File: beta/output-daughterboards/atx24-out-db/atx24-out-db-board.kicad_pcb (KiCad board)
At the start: 4 copper layers, 55 x 21.4 mm, 13 parts, among them J1 ATX24 OUT FIELD, J10 TE 63951-1, J11 TE 63951-1, J12 TE 63951-1, J13 TE 63951-1, J14 TE 63951-1, J15 TE 63951-1, J16 TE 63951-1, J17 TE 63951-1, J18 TE 63951-1, J19 TE 63951-1, J20 SIGNAL STUB (1x4 blind-mate)

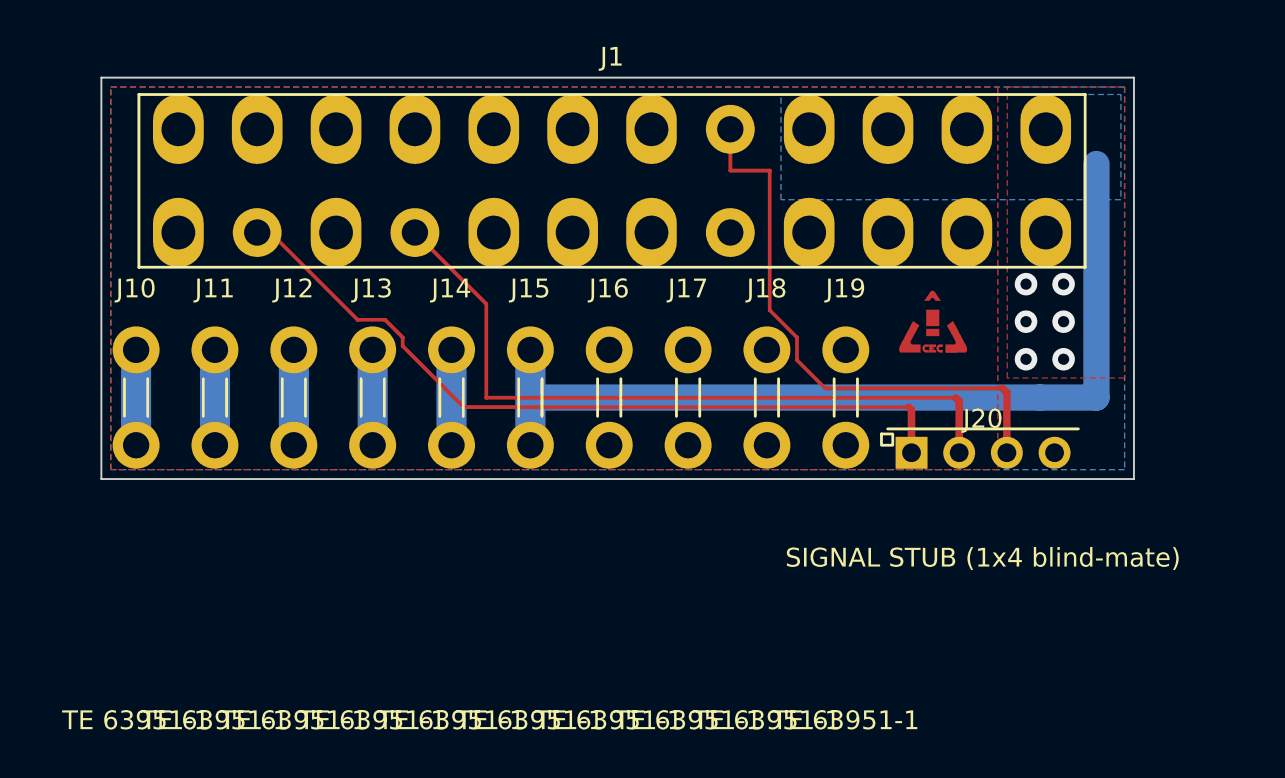
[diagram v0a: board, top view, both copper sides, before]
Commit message: Finalize compact Hub and ATX power-layout audit
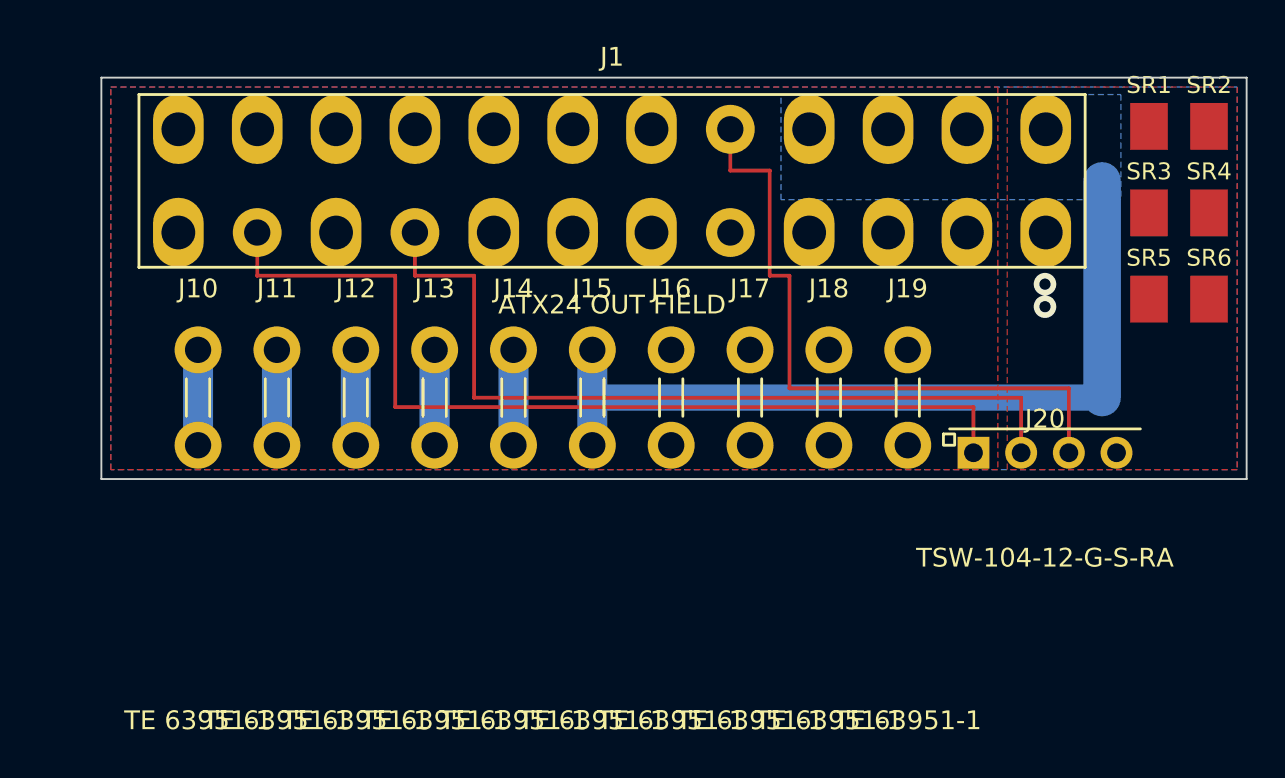
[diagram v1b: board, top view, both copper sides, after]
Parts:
- removed LOGO1: CEC_Logo_Copper_Small, cec:CEC_Logo_Copper_Small
- added SR1: SR_DNP, cec-Connector_Generic:CEC_SR_Pad_DNP, F.Cu at (55.8, 2.60)
- added SR2: SR_DNP, cec-Connector_Generic:CEC_SR_Pad_DNP, F.Cu at (59.0, 2.60)
- added SR3: SR_DNP, cec-Connector_Generic:CEC_SR_Pad_DNP, F.Cu at (55.8, 7.20)
- added SR4: SR_DNP, cec-Connector_Generic:CEC_SR_Pad_DNP, F.Cu at (59.0, 7.20)
- added SR5: SR_DNP, cec-Connector_Generic:CEC_SR_Pad_DNP, F.Cu at (55.8, 11.8)
- added SR6: SR_DNP, cec-Connector_Generic:CEC_SR_Pad_DNP, F.Cu at (59.0, 11.8)
- J20: value SIGNAL STUB (1x4 blind-mate) -> TSW-104-12-G-S-RA
- moved J19 3.30 mm to (43.0, 17.0)
- moved J20 3.30 mm to (46.5, 20.0)
- moved J12 3.30 mm to (13.6, 17.0)
- moved J13 3.30 mm to (17.8, 17.0)
- moved J14 3.30 mm to (21.9, 17.0)
- moved J16 3.30 mm to (30.4, 17.0)
- moved J10 3.30 mm to (5.15, 17.0)
- moved J11 3.30 mm to (9.35, 17.0)
- moved J15 3.30 mm to (26.1, 17.0)
- moved J17 3.30 mm to (34.5, 17.0)
- moved J18 3.30 mm to (38.8, 17.0)
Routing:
- net /-12V: track 41.3 -> 49.9 mm
- net /PS_ON#: track 38.4 -> 44.0 mm
- net /PWR_OK: track 30.1 -> 35.3 mm
- net +5VSB: track 47.7 -> 43.8 mm
- net +3V3: vias 6 -> 2
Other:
- board size 55 x 21.4 mm -> 61 x 21.4 mm

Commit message: pipeline: integrate route-aware physical design flow
Generalize critical-first placement and routing, future-congestion and power-authority planning, route provenance, process watchdogs, fab/thermal validation, dashboard review, and XFCN integration. Add the supporting board contracts, component libraries, documentation, and regression coverage.
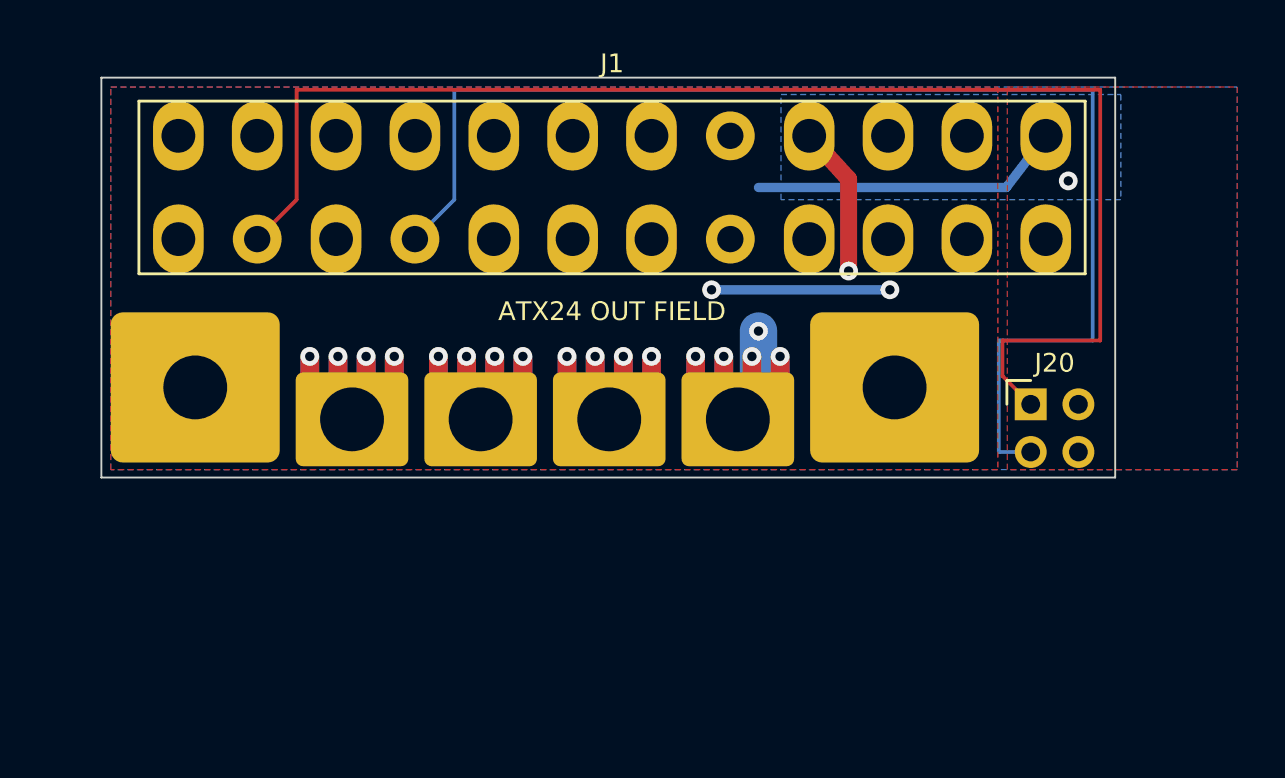
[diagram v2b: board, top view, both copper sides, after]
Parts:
- removed J12, J14, J17, J18: TE 63951-1, cec-Connector_Blade:TE_63951-1_FASTON_Tab_250x032_RA_THT
- removed SR1, SR2, SR3, SR4, SR5, SR6: SR_DNP, cec-Connector_Generic:CEC_SR_Pad_DNP
- J10, J11, J13, J15: value TE 63951-1 -> T34069 DB M3 PAD; footprint cec-Connector_Blade:TE_63951-1_FASTON_Tab_250x032_RA_THT -> cec-Connector_Screw:XFCN_T34069_Daughterboard_BoltPad_M3_PROVISIONAL
- J16, J19: value TE 63951-1 -> TTR32100127-0600 DB M3 PAD; footprint cec-Connector_Blade:TE_63951-1_FASTON_Tab_250x032_RA_THT -> cec-Connector_Screw:XFCN_TTR32100127-0600_Daughterboard_BoltPad_M3_PROVISIONAL
- J20: value TSW-104-12-G-S-RA -> TSW-102-16-G-D-RA; footprint cec-Connector_PinHeader_2.54mm:PinHeader_1x04_P2.54mm_Horizontal_LongPin -> cec-Connector_PinHeader_2.54mm:Samtec_TSW-102-16-G-D-RA_2x02_P2.54mm_Horizontal
- moved J16 25.4 mm to (5.00, 16.5)
- moved J10 21.9 mm to (27.1, 18.2)
- moved J11 10.9 mm to (20.2, 18.2)
- moved J15 7.84 mm to (33.9, 18.2)
- moved J13 4.55 mm to (13.3, 18.2)
- moved J20 3.99 mm to (49.5, 17.4)
- moved J19 0.88 mm to (42.2, 16.5)
- moved J1 0.35 mm to (4.10, 3.10)
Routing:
- net /PS_ON#: track 44.0 -> 68.8 mm
- net /-12V: track 49.9 -> 74.2 mm
- net +3V3: track 10.2 -> 27.5 mm, vias 2 -> 5
- net +5VSB: track 43.8 -> 28.8 mm, vias 0 -> 6
- net GND: track 0.00 -> 9.50 mm, vias 0 -> 2
- net +12V: track 5.08 -> 10.8 mm, vias 0 -> 4
- net /PWR_OK: track 35.3 -> 37.3 mm
- net +5V: track 10.2 -> 10.8 mm, vias 0 -> 4
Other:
- board size 61 x 21.4 mm -> 54 x 21.3 mm
